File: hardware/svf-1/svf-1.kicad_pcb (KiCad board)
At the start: 4 copper layers, 38.5 x 100 mm, 75 parts, among them J1 MonoJack, J2 MonoJack, J3 MonoJack, J4 MonoJack, J5 MonoJack, J6 MonoJack, J7 MonoJack, J8 MonoJack, J9 IDC Header 10P, Q1 MMDT5401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

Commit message: Schematic and PBC fix: replace incorrect MMDT5401 (SOT-363) with DMMT5401 (SOT-236) part
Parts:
- Q1: value MMDT5401 -> DMMT5401; footprint Package_TO_SOT_SMD:SOT-363_SC-70-6 -> Package_TO_SOT_SMD:SOT-23-6
- moved Q1 0.89 mm to (108.0, 77.7), turned to 180 degrees
- moved R26 0.26 mm to (105.7, 83.2)
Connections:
- Q1 pad 3: Net-(Q1B-C2) -> Net-(Q1B-B2)
- Q1 pad 5: Net-(Q1B-B2) -> Net-(Q1B-E2)
- R17 pad 1: Net-(Q1B-C2) -> Net-(Q1B-E2)
- R9 pad 1: Net-(Q1B-C2) -> Net-(Q1B-E2)
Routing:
- net Net-(Q1B-E2): track 0.00 -> 21.6 mm
- net Net-(Q1B-C2): track 19.7 -> 0.00 mm
- net Net-(Q1A-C1): track 12.4 -> 15.4 mm
- net Net-(Q1B-B2): track 4.88 -> 7.20 mm
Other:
- board text added: "v1.1.20251228"
- board text removed: "v1.0.20251214"

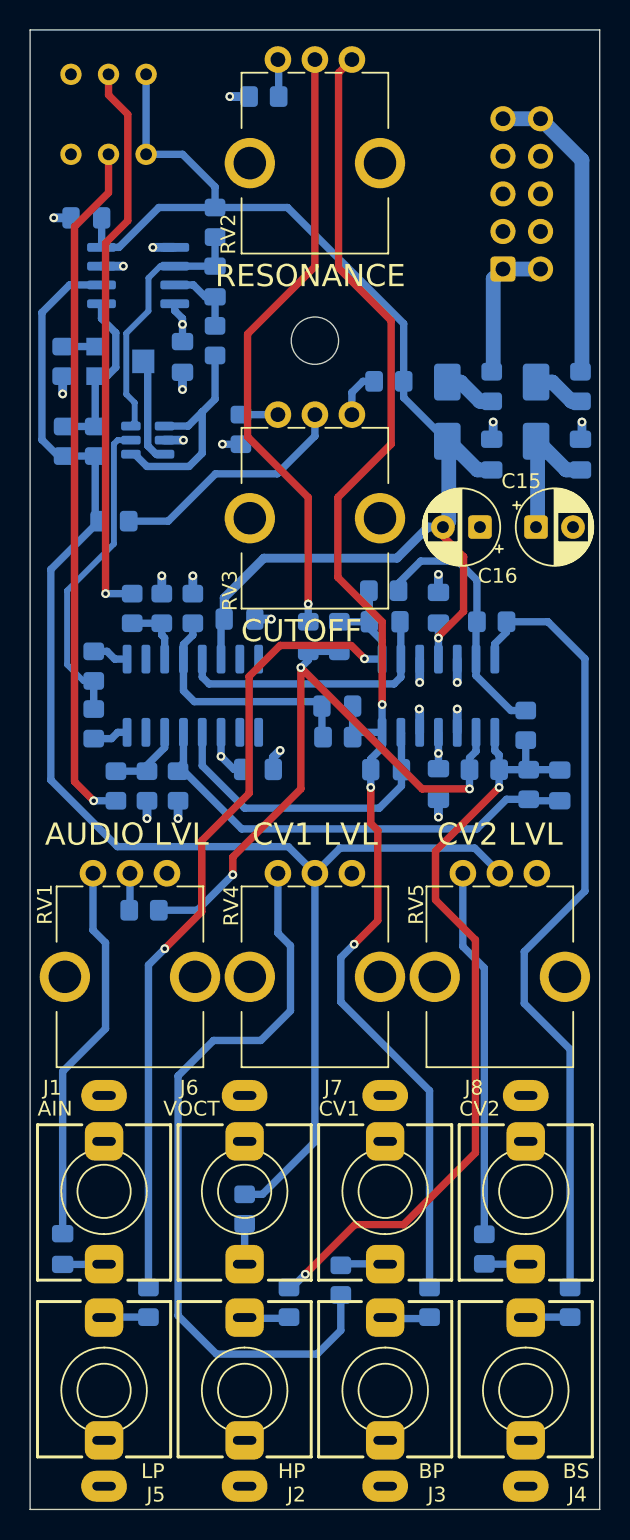
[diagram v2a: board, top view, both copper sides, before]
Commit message: Fix CV input pots and Rs
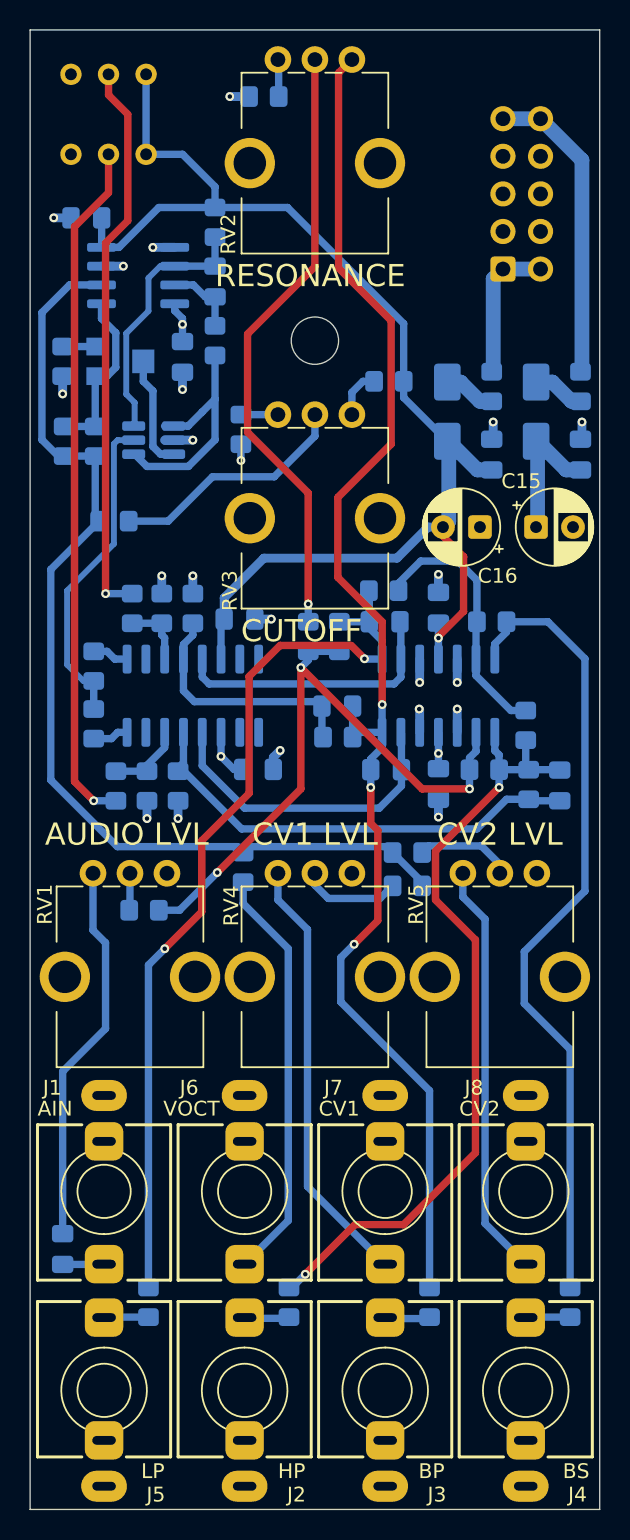
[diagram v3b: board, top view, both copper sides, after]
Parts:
- Q1: footprint Package_TO_SOT_SMD:SOT-23-6 -> Package_TO_SOT_SMD:SOT-23-6_Handsoldering
- R33, R34: value 100k -> 1M0
- moved R23 27.3 mm to (125.5, 105.6), turned to 180 degrees
- moved R25 27.0 mm to (125.5, 107.8), turned to 0 degrees
- moved R24 23.1 mm to (114.4, 106.6)
- moved Q1 0.40 mm to (108.3, 77.7)
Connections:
- R23 pad 1: Net-(J8-PadT) -> Net-(R23-Pad1)
- R23 pad 2: Net-(R23-Pad2) -> Net-(U3A--)
- R25 pad 1: Net-(J7-PadT) -> Net-(R25-Pad1)
- R25 pad 2: Net-(R25-Pad2) -> Net-(U3A--)
- RV4 pad 1: Net-(R25-Pad2) -> Net-(J7-PadT)
- RV4 pad 2: Net-(U3A--) -> Net-(R25-Pad1)
- RV5 pad 1: Net-(R23-Pad2) -> Net-(J8-PadT)
- RV5 pad 2: Net-(U3A--) -> Net-(R23-Pad1)
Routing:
- net Net-(R25-Pad2): track 50.4 -> 0.00 mm
- net Net-(U3A--): track 98.8 -> 68.6 mm
- net Net-(J7-PadT): track 2.91 -> 29.4 mm
- net Net-(J6-PadT): track 2.55 -> 28.3 mm
- net Net-(J8-PadT): track 2.81 -> 28.2 mm
- net Net-(R23-Pad2): track 25.0 -> 0.00 mm
- net Net-(R25-Pad1): track 0.00 -> 6.77 mm
- net Net-(R23-Pad1): track 0.00 -> 6.55 mm
- net Net-(Q1A-C1): track 15.4 -> 16.6 mm
- net Net-(U1A--): track 44.1 -> 43.4 mm
- net GND: track 27.5 -> 28.1 mm
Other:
- board text added: "v1.1.20260103"
- board text removed: "v1.1.20251228"

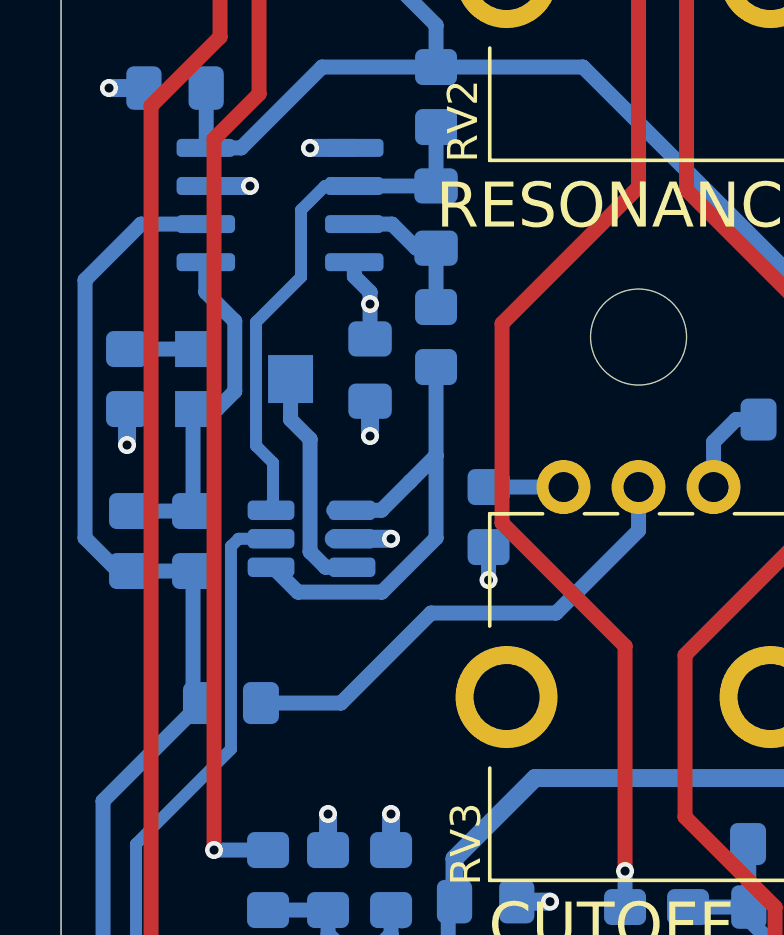
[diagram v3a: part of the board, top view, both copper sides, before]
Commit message: Fix for flipped PNP wiring
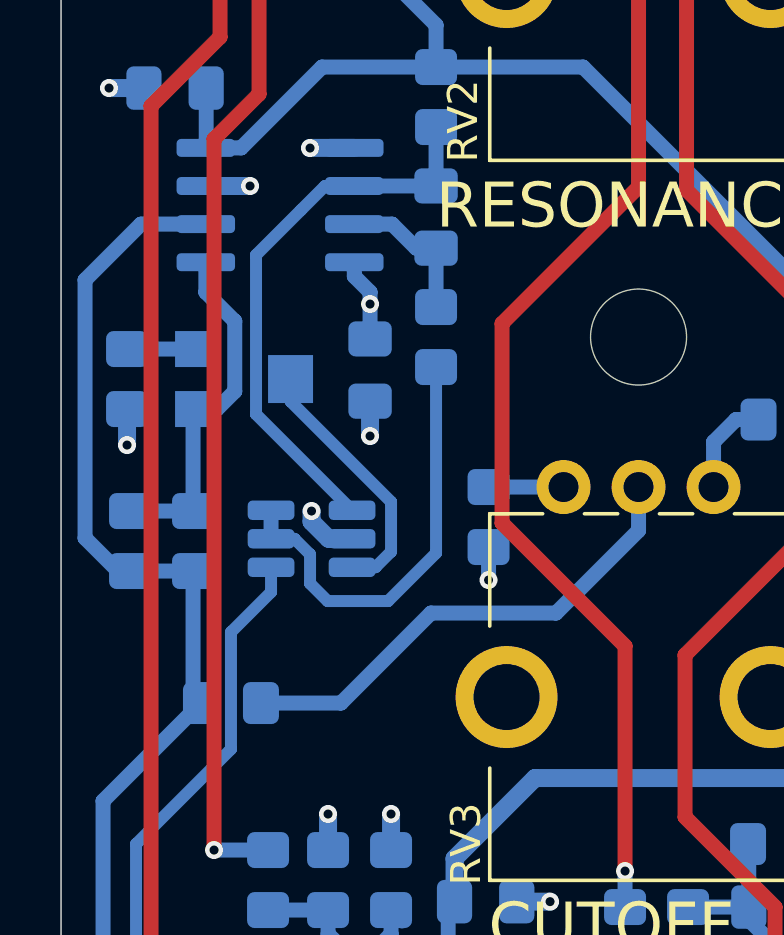
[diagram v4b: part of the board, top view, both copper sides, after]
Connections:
- C6 pad 1: Net-(Q1A-E1) -> Net-(Q1A-C1)
- Q1 pad 4: Net-(Q1A-C1) -> Net-(Q1B-C2)
- Q1 pad 5: Net-(Q1B-E2) -> Net-(Q1A-E1)
- R17 pad 1: Net-(Q1B-E2) -> Net-(Q1B-C2)
- R29 pad 2: Net-(Q1A-E1) -> Net-(Q1A-C1)
- R30 pad 1: Net-(Q1A-C1) -> Net-(Q1A-E1)
- R9 pad 1: Net-(Q1B-E2) -> Net-(Q1B-C2)
- U3 pad 6: Net-(Q1A-E1) -> Net-(Q1A-C1)
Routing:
- net Net-(Q1B-E2): track 21.6 -> 0.00 mm
- net Net-(Q1B-C2): track 0.00 -> 20.5 mm
- net Net-(Q1A-E1): track 17.8 -> 14.7 mm
- net Net-(Q1A-C1): track 16.6 -> 18.8 mm
- net Net-(Q1B-B2): track 7.03 -> 8.66 mm
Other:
- board text added: "v1.2.20260210"
- board text removed: "v1.1.20260103"
